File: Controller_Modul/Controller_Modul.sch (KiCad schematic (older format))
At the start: 140 parts, among them J101 Screw_Terminal_01x06, J102 Conn_02x01, J103 Conn_01x06_Male, J104 Conn_02x01, J105 Conn_01x04_Male, J106 Conn_01x08_Male, J107 Micro_SD_Card_Det, J108 IPC 16P, J109 Conn_02x20_Odd_Even, J110 USB_B_Mini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

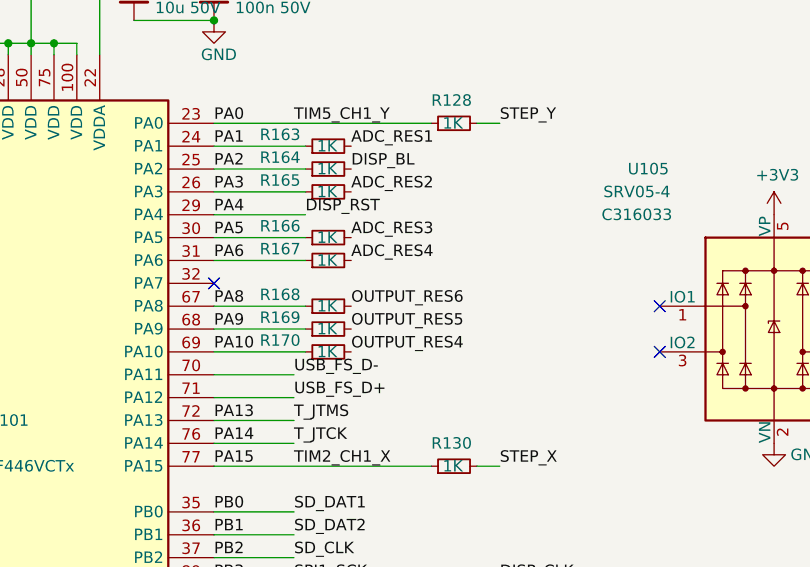
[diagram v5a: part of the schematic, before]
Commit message: ESD Protection für Feeder Modul USB hinzugefügt, Status LED für Controller Modul hinzugefügt
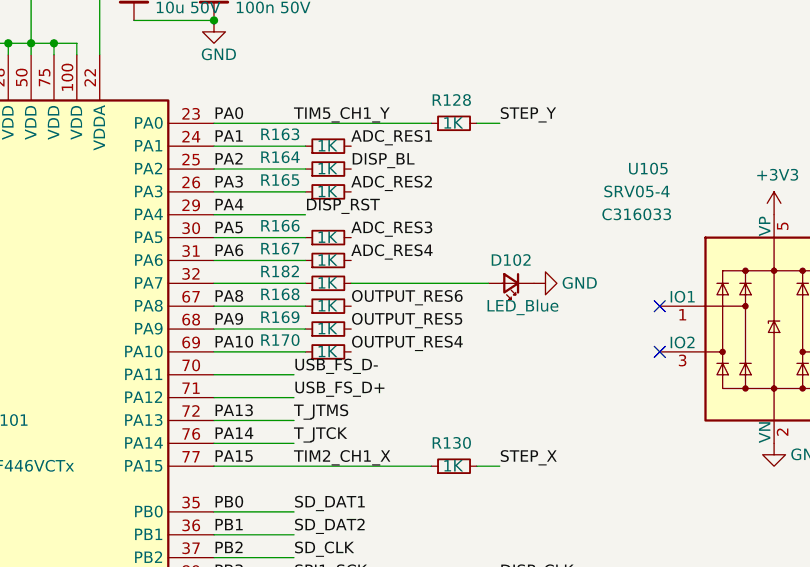
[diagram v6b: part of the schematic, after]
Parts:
- added D102: LED_Blue, LED_SMD:LED_0603_1608Metric, symbol Device:LED_Small
- added R182: 1K, Resistor_SMD:R_0603_1608Metric, symbol Device:R_Small
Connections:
- net GND: now also D102.1 (K)
- net at U101.32 (PA7): now also R182.1
- new net: D102.2 (A), R182.2
- no-connect marks 10 -> 9
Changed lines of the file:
@@
 Wire Wire Line
 	3300 7850 3400 7850
-NoConn ~ 4300 3450
 $Comp
 L Device:R_Small R?
@@
 Wire Wire Line
 	1450 2750 2250 2750
+$Comp
+L Device:R_Small R?
+U 1 1 602E06B7
+P 4800 3450
+AR Path="/5FDD0F66/602E06B7" Ref="R?"  Part="1"
+AR Path="/602E06B7" Ref="R182"  Part="1"
+F 0 "R182" V 4850 3750 50  0000 R CNN
+F 1 "1K" V 4800 3500 50  0000 R CNN
+F 2 "Resistor_SMD:R_0603_1608Metric" H 4800 3450 50  0001 C CNN
+F 3 "~" H 4800 3450 50  0001 C CNN
+F 4 "C14676" H 4800 3450 50  0001 C CNN "LCSC"
+	1    4800 3450
+	0    -1   -1   0
+$EndComp
+Wire Wire Line
+	4700 3450 4300 3450
+$Comp
+L Device:LED_Small D102
+U 1 1 6026FBC3
+P 5600 3450
+F 0 "D102" H 5600 3350 50  0000 C CNN
+F 1 "LED_Blue" H 5550 3550 50  0000 C CNN
+F 2 "LED_SMD:LED_0603_1608Metric" V 5600 3450 50  0001 C CNN
+F 3 "https://datasheet.lcsc.com/szlcsc/TOGIALED-TJ-S1608SW6TGLC6B-A5_C192317.pdf" V 5600 3450 50  0001 C CNN
+F 4 "C192317" H 5600 3450 50  0001 C CNN "LCSC"
+	1    5600 3450
+	-1   0    0    1
+$EndComp
+Wire Wire Line
+	5500 3450 4900 3450
+$Comp
+L power:GND #PWR?
+U 1 1 602934CC
+P 5700 3450
+AR Path="/5FDD0F66/602934CC" Ref="#PWR?"  Part="1"
+AR Path="/602934CC" Ref="#PWR0181"  Part="1"
+F 0 "#PWR0181" H 5700 3200 50  0001 C CNN
+F 1 "GND" V 5700 3250 50  0000 C CNN
+F 2 "" H 5700 3450 50  0001 C CNN
+F 3 "" H 5700 3450 50  0001 C CNN
+	1    5700 3450
+	0    -1   -1   0
+$EndComp
 $EndSCHEMATC

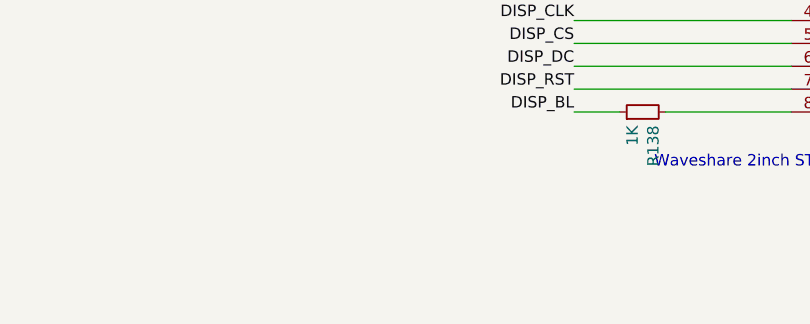
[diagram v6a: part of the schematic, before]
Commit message: Fiducials auf allen Boards hinzugefügt
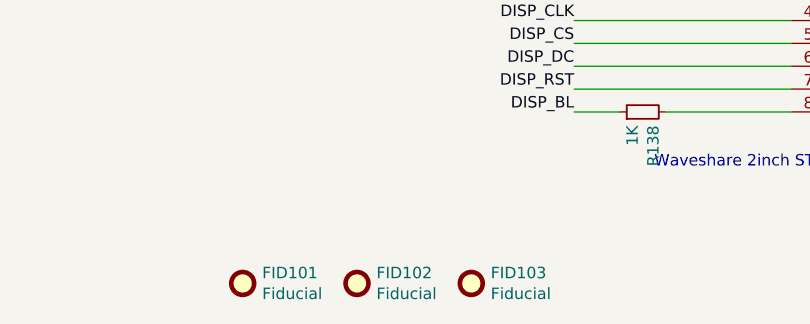
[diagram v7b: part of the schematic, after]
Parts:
- added FID101, FID102, FID103: Fiducial, Fiducial:Fiducial_1mm_Mask2mm, symbol Mechanical:Fiducial
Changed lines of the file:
@@
 	0    -1   -1   0
 $EndComp
+$Comp
+L Mechanical:Fiducial FID101
+U 1 1 6021DC68
+P 6500 10500
+F 0 "FID101" H 6585 10546 50  0000 L CNN
+F 1 "Fiducial" H 6585 10455 50  0000 L CNN
+F 2 "Fiducial:Fiducial_1mm_Mask2mm" H 6500 10500 50  0001 C CNN
+F 3 "~" H 6500 10500 50  0001 C CNN
+	1    6500 10500
+	1    0    0    -1
+$EndComp
+$Comp
+L Mechanical:Fiducial FID102
+U 1 1 60223FCE
+P 7000 10500
+F 0 "FID102" H 7085 10546 50  0000 L CNN
+F 1 "Fiducial" H 7085 10455 50  0000 L CNN
+F 2 "Fiducial:Fiducial_1mm_Mask2mm" H 7000 10500 50  0001 C CNN
+F 3 "~" H 7000 10500 50  0001 C CNN
+	1    7000 10500
+	1    0    0    -1
+$EndComp
+$Comp
+L Mechanical:Fiducial FID103
+U 1 1 60224658
+P 7500 10500
+F 0 "FID103" H 7585 10546 50  0000 L CNN
+F 1 "Fiducial" H 7585 10455 50  0000 L CNN
+F 2 "Fiducial:Fiducial_1mm_Mask2mm" H 7500 10500 50  0001 C CNN
+F 3 "~" H 7500 10500 50  0001 C CNN
+	1    7500 10500
+	1    0    0    -1
+$EndComp
 $EndSCHEMATC

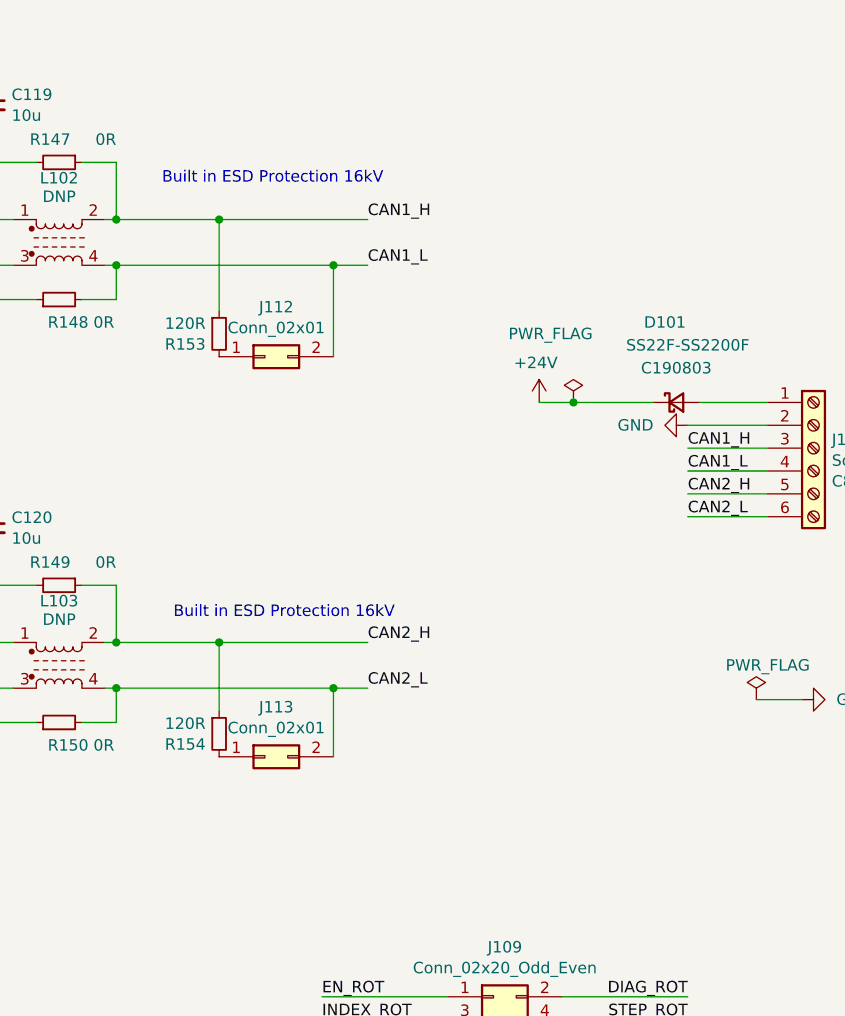
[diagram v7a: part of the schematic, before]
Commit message: ESD Protection überarbeitet, aber noch nicht fertig
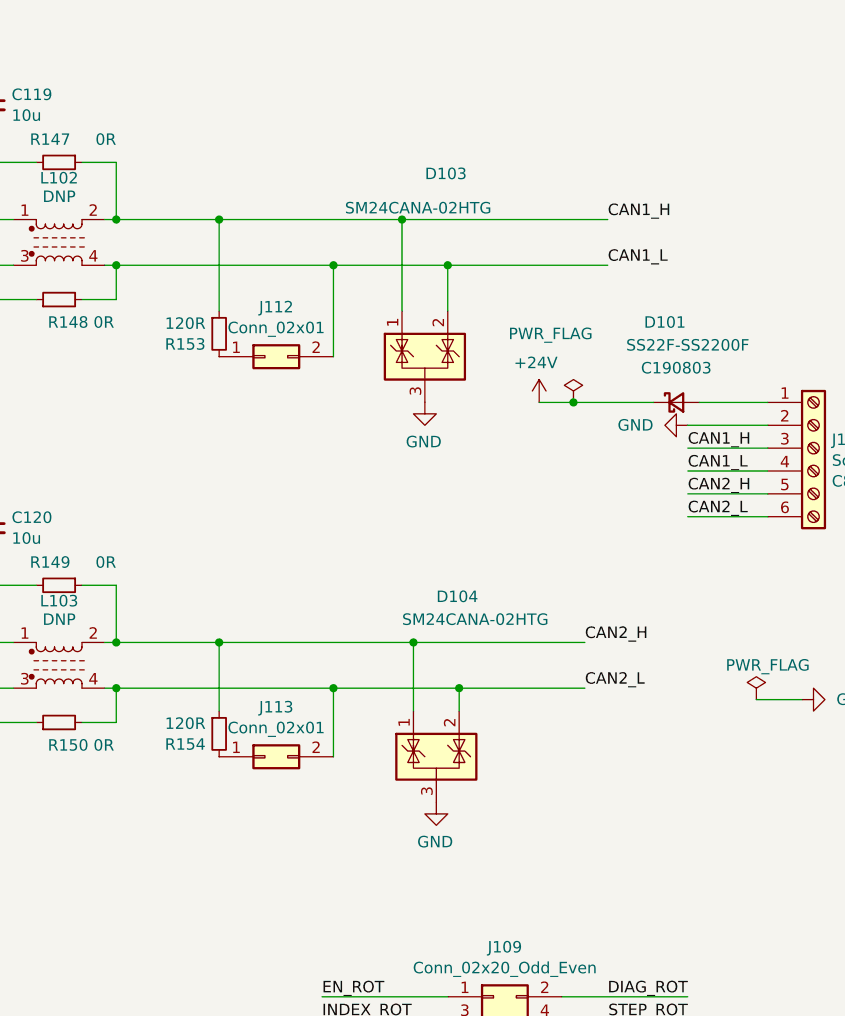
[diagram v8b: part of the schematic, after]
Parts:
- added D103, D104: SM24CANA-02HTG, Package_TO_SOT_SMD:SOT-23, symbol Power_Protection:NUP2105L
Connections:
- net CAN1_H: now also D103.1 (K)
- net CAN1_L: now also D103.2 (K)
- net CAN2_H: now also D104.1 (K)
- net CAN2_L: now also D104.2 (K)
- net GND: now also D103.3 (A), D104.3 (A)
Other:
- note removed: "Built in ESD Protection 16kV"
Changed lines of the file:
@@
 Wire Wire Line
 	14900 2950 15250 2950
-Text Label 13500 1650 0    50   ~ 0
+Text Label 14550 1650 0    50   ~ 0
 CAN1_H
-Text Label 13500 1850 0    50   ~ 0
+Text Label 14550 1850 0    50   ~ 0
 CAN1_L
-Text Label 13500 3500 0    50   ~ 0
+Text Label 14450 3500 0    50   ~ 0
 CAN2_H
-Text Label 13500 3700 0    50   ~ 0
+Text Label 14450 3700 0    50   ~ 0
 CAN2_L
 $Comp
@@
 Connection ~ 12850 1650
 Wire Wire Line
-	12850 1650 13500 1650
+	12850 1650 13650 1650
 Wire Wire Line
 	13350 2250 13350 1850
 Connection ~ 13350 1850
 Wire Wire Line
-	13350 1850 13500 1850
+	13350 1850 13850 1850
 $Comp
 L Connector_Generic:Conn_02x01 J?
@@
 Connection ~ 12850 3500
 Wire Wire Line
-	12850 3500 13500 3500
+	12850 3500 13700 3500
 Wire Wire Line
 	13350 4000 13350 3700
 Connection ~ 13350 3700
 Wire Wire Line
-	13350 3700 13500 3700
-Text Notes 12600 1500 0    50   ~ 0
-Built in ESD Protection 16kV
-Text Notes 12650 3400 0    50   ~ 0
-Built in ESD Protection 16kV
+	13350 3700 13900 3700
 Text Notes 9700 2400 0    50   ~ 0
 High Speed Mode
@@
 	1    0    0    -1
 $EndComp
+$Comp
+L Power_Protection:NUP2105L D104
+U 1 1 60571CCA
+P 13800 4000
+F 0 "D104" H 13800 4700 50  0000 L CNN
+F 1 "SM24CANA-02HTG" H 13650 4600 50  0000 L CNN
+F 2 "Package_TO_SOT_SMD:SOT-23" H 14025 3950 50  0001 L CNN
+F 3 "http://www.onsemi.com/pub_link/Collateral/NUP2105L-D.PDF" H 13925 4125 50  0001 C CNN
+F 4 "C151236" H 13800 4000 50  0001 C CNN "LCSC"
+	1    13800 4000
+	1    0    0    -1
+$EndComp
+$Comp
+L power:GND #PWR0182
+U 1 1 60571CD0
+P 13800 4200
+F 0 "#PWR0182" H 13800 3950 50  0001 C CNN
+F 1 "GND" H 13805 4027 50  0000 C CNN
+F 2 "" H 13800 4200 50  0001 C CNN
+F 3 "" H 13800 4200 50  0001 C CNN
+	1    13800 4200
+	-1   0    0    -1
+$EndComp
+Wire Wire Line
+	13700 3800 13700 3500
+Connection ~ 13700 3500
+Wire Wire Line
+	13700 3500 14450 3500
+Wire Wire Line
+	13900 3800 13900 3700
+Connection ~ 13900 3700
+Wire Wire Line
+	13900 3700 14450 3700
+$Comp
+L Power_Protection:NUP2105L D103
+U 1 1 6072B4A3
+P 13750 2250
+F 0 "D103" H 13750 3050 50  0000 L CNN
+F 1 "SM24CANA-02HTG" H 13400 2900 50  0000 L CNN
+F 2 "Package_TO_SOT_SMD:SOT-23" H 13975 2200 50  0001 L CNN
+F 3 "http://www.onsemi.com/pub_link/Collateral/NUP2105L-D.PDF" H 13875 2375 50  0001 C CNN
+F 4 "C151236" H 13750 2250 50  0001 C CNN "LCSC"
+	1    13750 2250
+	1    0    0    -1
+$EndComp
+$Comp
+L power:GND #PWR0183
+U 1 1 6072BC55
+P 13750 2450
+F 0 "#PWR0183" H 13750 2200 50  0001 C CNN
+F 1 "GND" H 13755 2277 50  0000 C CNN
+F 2 "" H 13750 2450 50  0001 C CNN
+F 3 "" H 13750 2450 50  0001 C CNN
+	1    13750 2450
+	-1   0    0    -1
+$EndComp
+Wire Wire Line
+	13650 2050 13650 1650
+Connection ~ 13650 1650
+Wire Wire Line
+	13650 1650 14550 1650
+Wire Wire Line
+	13850 2050 13850 1850
+Connection ~ 13850 1850
+Wire Wire Line
+	13850 1850 14550 1850
 $EndSCHEMATC
